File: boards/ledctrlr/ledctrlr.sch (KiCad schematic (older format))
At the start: 56 parts, among them IC1 ATMEGA168-P, IC2 SN75176B, J1 RJ45, J2 RJ45, SW1 SW_PUSH, U1 LM7805, X1 CRYSTAL

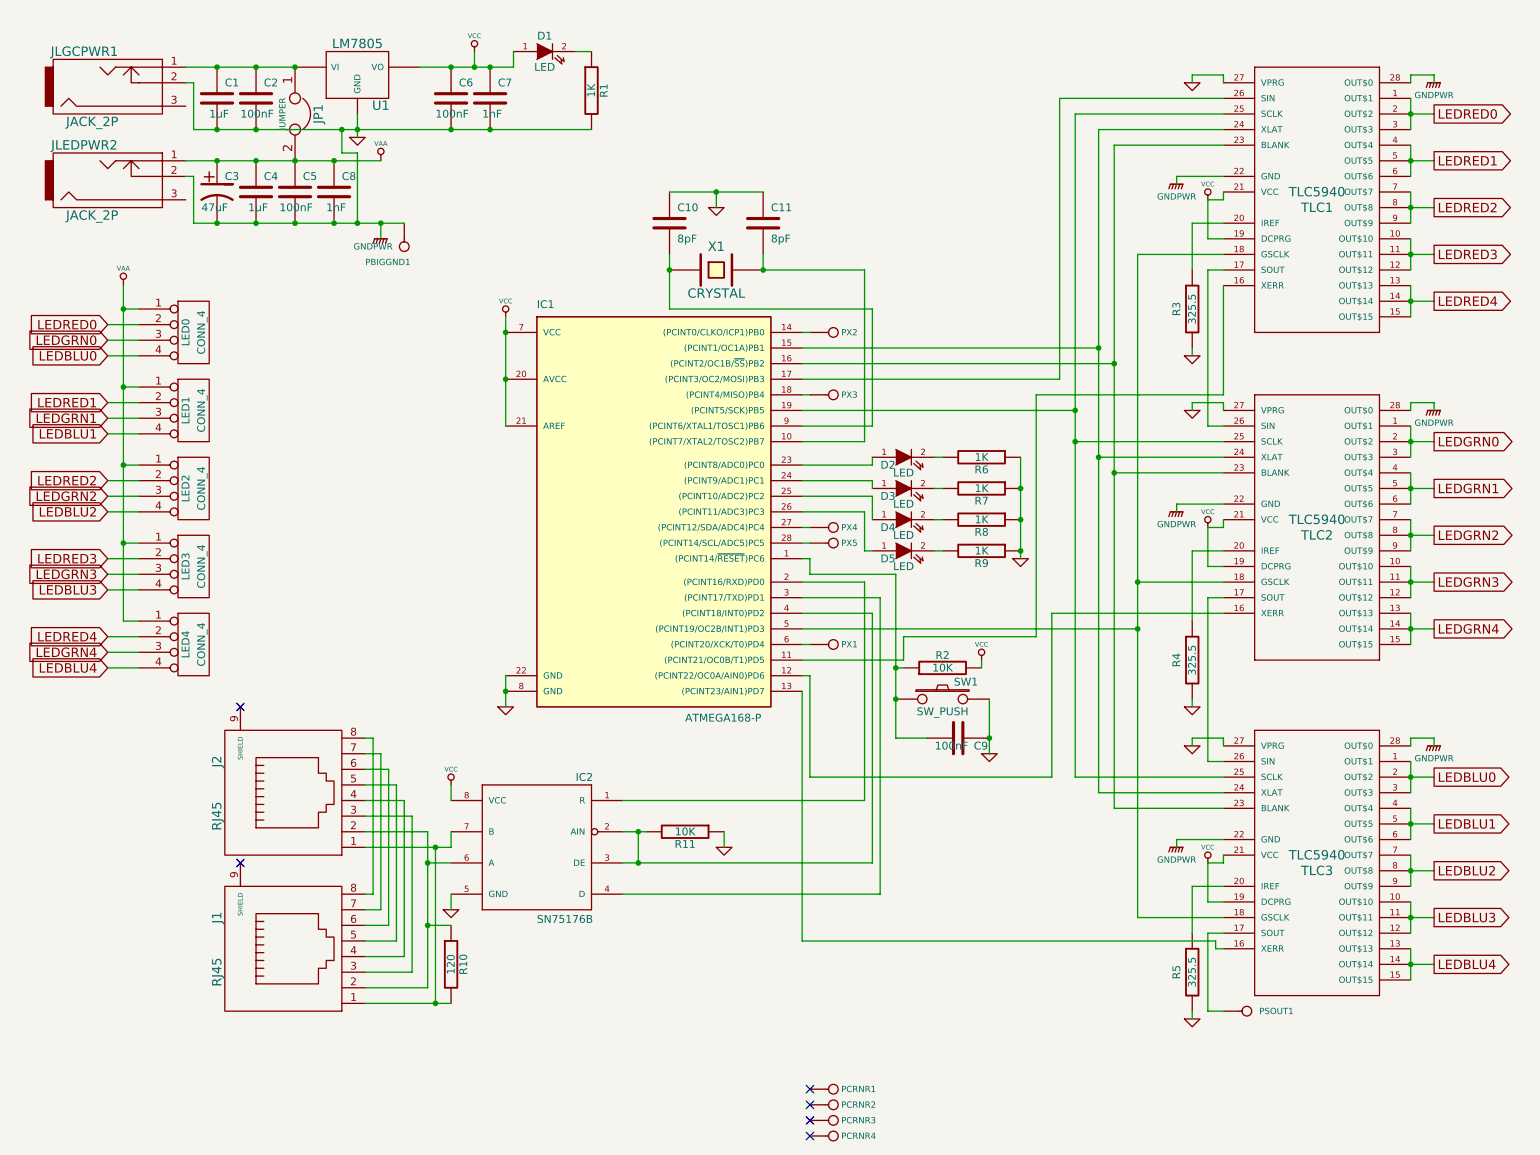
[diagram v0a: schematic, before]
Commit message: Potential new board layout... needs routing
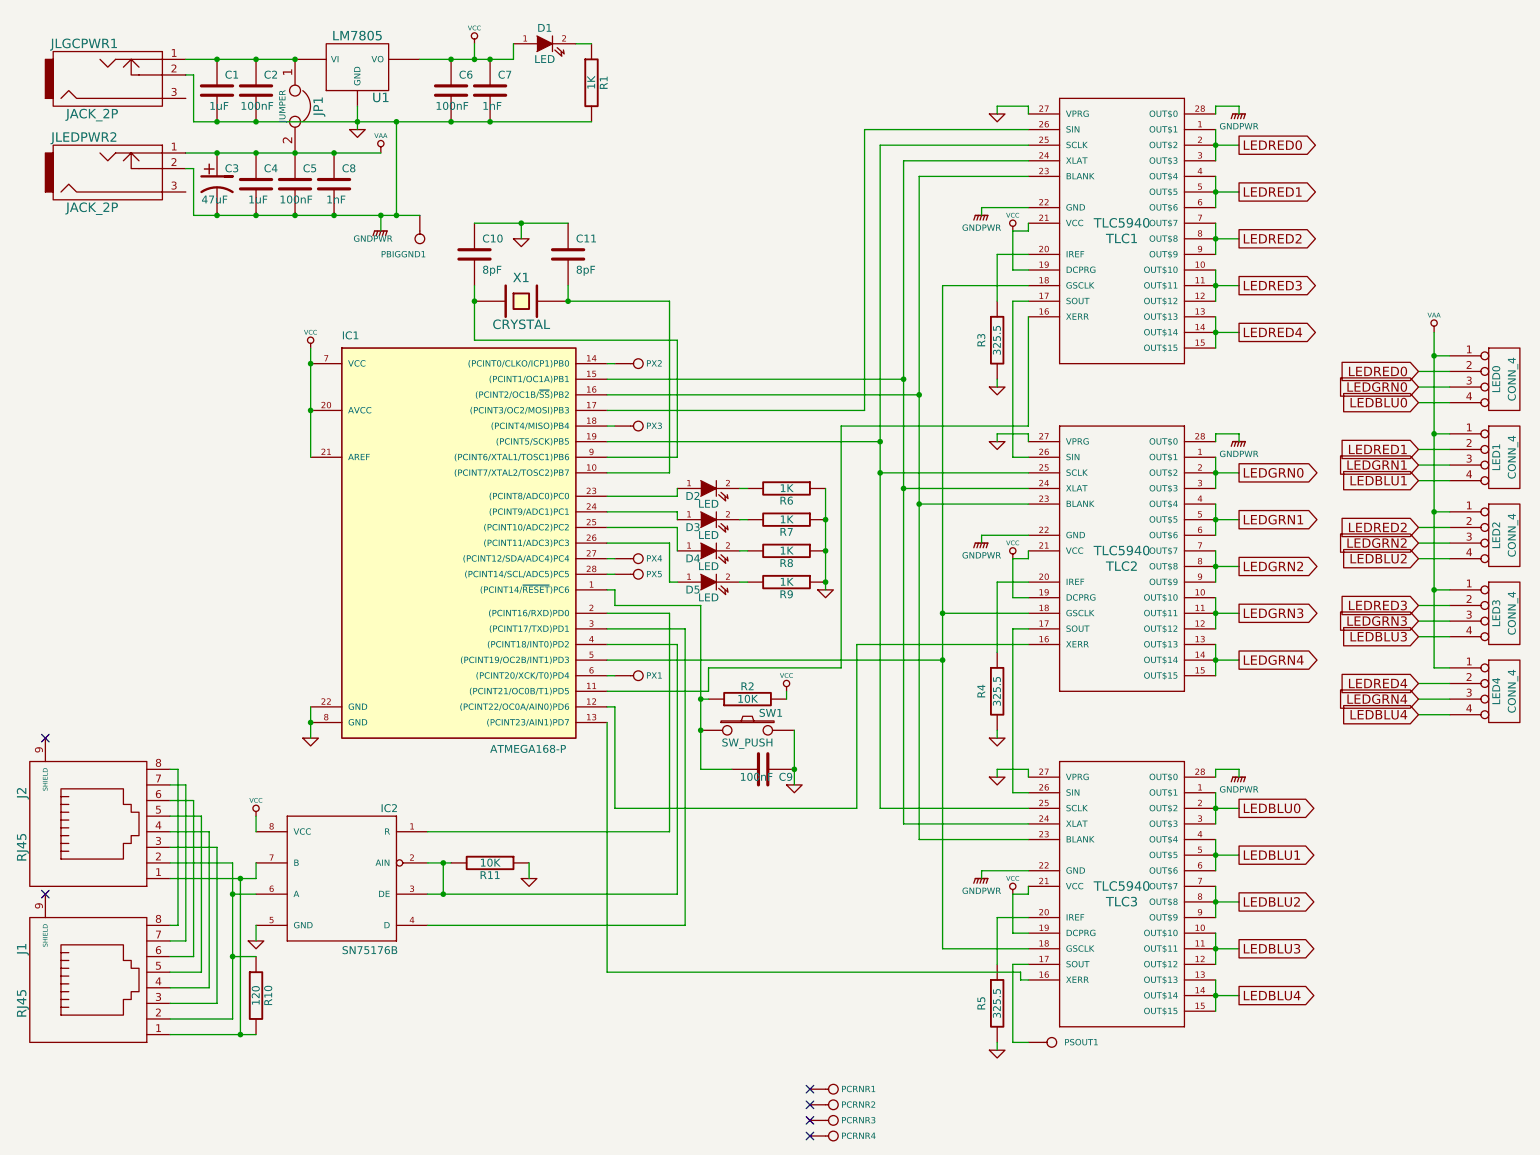
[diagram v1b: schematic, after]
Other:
- moved on the sheet: C1, C10, C11, C2, C3, C4, C5, C6, C7, C8, C9, D1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

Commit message: placement of v2.0 boards almost done
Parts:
- removed C1: 1uF, C1, symbol C
- removed C11: 8pF, SM0805, symbol C
- removed C6: 100nF, C1, symbol C
- removed C8: 1nF, C1, symbol C
- removed C9: 100nF, SM0805, symbol C
- added C2: .33uF, SM0805, symbol C
- added PPWR1, PVCC1: CONN_1, PAD, symbol CONN_1
- C1: renamed from C2; value 100nF -> .33uF; footprint C1 -> SM0805; DigikeyPart 478-4862-ND -> 445-1356-1-ND; Part SR215C103KAR -> C2012X7R1C334K/1.25
- C3: value 47uF -> 100uF; DigikeyPart P5137-ND -> 399-6103-ND; Part ECA-1CM470 -> ESK107M025AE3AA
- C4: value 1uF -> .1uF; footprint C1 -> SM0805; DigikeyPart 478-5812-ND -> 311-1361-1-ND; Part TAP105M035SCS -> CC0805ZRY5V9BB104
- C5: value 100nF -> .1uF; footprint C1 -> SM0805; DigikeyPart 478-1831-ND -> 311-1361-1-ND; Part TAP104K035SCS -> CC0805ZRY5V9BB104
- C6: renamed from C10; Part CC0805DRNP09BN8R0 -> CC0805DRNPO9BN8R0
- C7: value 1nF -> 8pF; footprint C1 -> SM0805; DigikeyPart 478-4862-ND -> 311-1097-1-ND; Part SR215C103KAR -> CC0805DRNPO9BN8R0
- D1, D2, D3, D4, D5: footprint LED-1206 -> LED-1206-3D
- IC2: footprint DIP-8__300 -> SOIC8
- LED0, LED1, LED2, LED3, LED4: footprint (none) -> OSTTA040161
- PGND1: renamed from PBIGGND1; footprint 1pin -> PAD
- PSOUT1, PX1, PX2, PX3, PX4, PX5: footprint SIL-1 -> PAD
- R11: footprint (none) -> SM0805
- TLC1, TLC2, TLC3: footprint DIP-28__300 -> tssop-28-thermal
- U1: footprint LM78XXV -> LM78XXV-3D
- X1: footprint Crystal_FOX-FE-SMD-RevA_09Aug201 -> Crystal_FOX-FE_SMD_RevA_09Aug2010
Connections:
- net GND: now also C6.2, JLEDPWR2.3, JLGCPWR1.3, R11.2, R6.2, R7.2, R8.2, R9.2, C2.2; no longer C6.1, R11.1, R6.1, R7.1, R8.1, R9.1
- net VAA: now also C2.1, PPWR1.1; no longer C4.1, C5.1
- net VCC: now also C4.1, R2.1, PVCC1.1; no longer C7.1, R2.2
- net at IC1.4 ((PCINT18/INT0)PD2), IC2.2 (AIN), IC2.3 (DE): now also R11.1; no longer R11.2
- net at IC2.6 (A), J1.2, J2.2: now also R10.2; no longer R10.1
- net at IC2.7 (B), J1.1, J2.1: now also R10.1; no longer R10.2
- net at IC1.9 ((PCINT6/XTAL1/TOSC1)PB6), X1.1: now also C6.1; no longer C6.2
- net at IC1.10 ((PCINT7/XTAL2/TOSC2)PB7), X1.2: now also C7.1
- net at IC1.1 ((PCINT14/~RESET~)PC6), SW1.1: now also C5.1, R2.2; no longer R2.1
- net at D2.2 (K): now also R6.1; no longer R6.2
- net at D3.2 (K): now also R7.1; no longer R7.2
- net at D4.2 (K): now also R8.1; no longer R8.2
- net at D5.2 (K): now also R9.1; no longer R9.2
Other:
- moved on the sheet: C1, C3, C6, D1, D2, D3, D4, D5, IC1, IC2, J1, J2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

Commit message: ran into unroutable issue, I think -- try with freeroute
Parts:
- PCRNR1, PCRNR2, PCRNR3, PCRNR4: footprint 1pin -> screw
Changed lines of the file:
@@
-EESchema Schematic File Version 2  date Sat 24 Mar 2012 09:28:25 PM EDT
+EESchema Schematic File Version 2  date Sun 25 Mar 2012 02:40:29 PM EDT
 LIBS:power
 LIBS:device
@@
 F 0 "PCRNR4" H 6000 7800 40  0000 L CNN
 F 1 "CONN_1" H 5950 7855 30  0001 C CNN
-F 2 "1pin" H 6040 7760 60  0001 C CNN
+F 2 "screw" H 6040 7760 60  0001 C CNN
 F 4 "N/A" H 5950 7800 60  0001 C CNN "Part"
 F 5 "N/A" H 5950 7800 60  0001 C CNN "DigikeyPart"
@@
 F 0 "PCRNR3" H 6000 7700 40  0000 L CNN
 F 1 "CONN_1" H 5950 7755 30  0001 C CNN
-F 2 "1pin" H 6040 7660 60  0001 C CNN
+F 2 "screw" H 6040 7660 60  0001 C CNN
 F 4 "N/A" H 5950 7700 60  0001 C CNN "Part"
 F 5 "N/A" H 5950 7700 60  0001 C CNN "DigikeyPart"
@@
 F 0 "PCRNR2" H 6000 7600 40  0000 L CNN
 F 1 "CONN_1" H 5950 7655 30  0001 C CNN
-F 2 "1pin" H 6040 7560 60  0001 C CNN
+F 2 "screw" H 6040 7560 60  0001 C CNN
 F 4 "N/A" H 5950 7600 60  0001 C CNN "Part"
 F 5 "N/A" H 5950 7600 60  0001 C CNN "DigikeyPart"
@@
 F 0 "PCRNR1" H 6000 7500 40  0000 L CNN
 F 1 "CONN_1" H 5950 7555 30  0001 C CNN
-F 2 "1pin" H 6040 7460 60  0001 C CNN
+F 2 "screw" H 6040 7460 60  0001 C CNN
 F 4 "N/A" H 5950 7500 60  0001 C CNN "Part"
 F 5 "N/A" H 5950 7500 60  0001 C CNN "DigikeyPart"
